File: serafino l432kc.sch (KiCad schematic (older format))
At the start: 31 parts, among them J1 USB_B_Micro, J2 Conn_01x14, J3 Conn_01x14, Q1 SI3401A-TP, SW1 SW_Push, SW2 SW_Push, U1 AP2112K-3.3, U2 USBLC6-2SC6, U3 STM32L432KCUx, Y1 32.768K

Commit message: Avances
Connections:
- net BOOT0: no longer J2.13 (Pin_13)
- net EN: no longer J2.2 (Pin_2)
- net PA8: now also J2.13 (Pin_13); no longer J3.4 (Pin_4)
- net VHIGH: now also J2.2 (Pin_2); no longer J2.3 (Pin_3)
- net USB_D+ renamed CAN_TD
- net CAN_TD: now also J2.3 (Pin_3)
- net USB_D- renamed CAN_RD
- net CAN_RD: now also J3.4 (Pin_4)
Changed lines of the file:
@@
 Text GLabel 6700 4800 2    50   Input ~ 0
 SWCLK
-Text GLabel 6700 4600 2    50   Input ~ 0
+Text GLabel 7350 4700 2    50   Input ~ 0
 USB_D+
-Text GLabel 6700 4500 2    50   Input ~ 0
+Text GLabel 7350 4400 2    50   Input ~ 0
 USB_D-
 Text GLabel 5700 4800 0    50   Input ~ 0
@@
 	1    0    0    -1
 $EndComp
-Text GLabel 8750 3650 0    50   Input ~ 0
+Text GLabel 8750 3550 0    50   Input ~ 0
 VHIGH
 Text GLabel 8750 4750 0    50   Input ~ 0
 NRST
-Text GLabel 10250 3750 0    50   Input ~ 0
+Text GLabel 8750 4650 0    50   Input ~ 0
 PA8
 Text GLabel 8750 4050 0    50   Input ~ 0
@@
 Text GLabel 10250 3950 0    50   Input ~ 0
 SPI1_SS
-Text GLabel 8750 4250 0    50   Input ~ 0
-PB4
 Text GLabel 10250 4650 0    50   Input ~ 0
 LED0
@@
 Text GLabel 10250 4350 0    50   Input ~ 0
 SAI1_FS_B
-Text GLabel 8750 4550 0    50   Input ~ 0
-USART1_RX
-Text GLabel 8750 4450 0    50   Input ~ 0
-USART1_TX
 Text GLabel 10250 4250 0    50   Input ~ 0
 SPI1_SCK
@@
 Wire Wire Line
 	8500 3450 8750 3450
-Text GLabel 8750 4650 0    50   Input ~ 0
-BOOT0
 $Comp
 L Device:R_Small R3
@@
 Text GLabel 8750 4150 0    50   Input ~ 0
 SAI1_SCK_B
-Text GLabel 8750 3550 0    50   Input ~ 0
-EN
 Wire Wire Line
 	2250 4600 2900 4600
@@
 Text GLabel 5700 4700 0    50   Input ~ 0
 SAI1_SD_B
-Text GLabel 8750 4350 0    50   Input ~ 0
-SAI1_SD_B
-$Comp
-L power:+3.3V #PWR?
+$Comp
+L power:+3.3V #PWR0107
 U 1 1 6018DE27
 P 3850 5700
-F 0 "#PWR?" H 3850 5550 50  0001 C CNN
+F 0 "#PWR0107" H 3850 5550 50  0001 C CNN
 F 1 "+3.3V" H 3865 5873 50  0000 C CNN
 F 2 "" H 3850 5700 50  0001 C CNN
@@
 Text Notes 1500 6100 0    50   ~ 0
 * LED for Native \nDFU Mode Indicator
+Text GLabel 8750 4250 0    50   Input ~ 0
+PB4
+Text GLabel 8750 4350 0    50   Input ~ 0
+SAI1_SD_B
+Text GLabel 8750 4450 0    50   Input ~ 0
+USART1_TX
+Text GLabel 8750 4550 0    50   Input ~ 0
+USART1_RX
+Text GLabel 8750 3650 0    50   Input ~ 0
+CAN_TD
+Text GLabel 10250 3750 0    50   Input ~ 0
+CAN_RD
+Wire Wire Line
+	7350 4400 7250 4400
+Wire Wire Line
+	7250 4400 7250 4500
+Wire Wire Line
+	7250 4500 6700 4500
+Wire Wire Line
+	7350 4700 7250 4700
+Wire Wire Line
+	7250 4700 7250 4600
+Wire Wire Line
+	7250 4600 6700 4600
+Text GLabel 7350 4850 2    50   Input ~ 0
+CAN_TD
+Text GLabel 7350 4250 2    50   Input ~ 0
+CAN_RD
+Wire Wire Line
+	7350 4250 7250 4250
+Wire Wire Line
+	7250 4250 7250 4400
+Connection ~ 7250 4400
+Wire Wire Line
+	7350 4850 7250 4850
+Wire Wire Line
+	7250 4850 7250 4700
+Connection ~ 7250 4700
 $EndSCHEMATC

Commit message: Finished back labels
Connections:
- net EN: no longer names the net of R5.2, U1.3 (EN)
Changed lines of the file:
@@
 Wire Wire Line
 	2500 1850 2500 1700
-Text GLabel 2500 1950 3    50   Input ~ 0
-EN
-Wire Wire Line
-	2500 1950 2500 1850
-Connection ~ 2500 1850
 Wire Wire Line
 	8000 3650 8000 3750

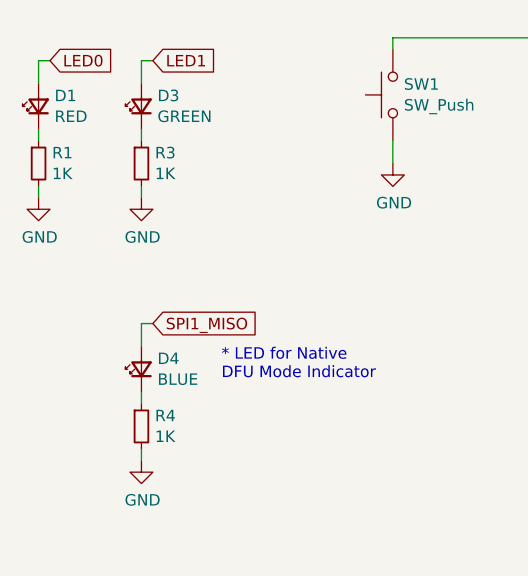
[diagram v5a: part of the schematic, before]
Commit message: Adjusted LED resistor values, changed BOOT0 to PA0 in silk screen.
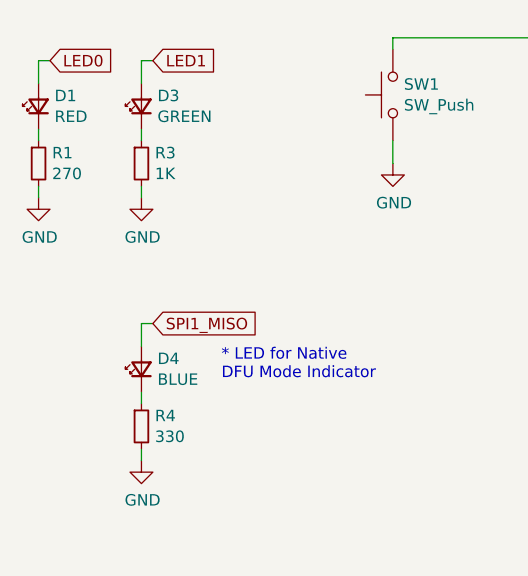
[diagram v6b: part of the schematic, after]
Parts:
- R1: value 1K -> 270
- R4: value 1K -> 330
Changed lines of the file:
@@
 P 700 5150
 F 0 "R1" H 759 5196 50  0000 L CNN
-F 1 "1K" H 759 5105 50  0000 L CNN
+F 1 "270" H 759 5105 50  0000 L CNN
 F 2 "Resistor_SMD:R_0603_1608Metric" H 700 5150 50  0001 C CNN
 F 3 "~" H 700 5150 50  0001 C CNN
@@
 P 1150 6300
 F 0 "R4" H 1209 6346 50  0000 L CNN
-F 1 "1K" H 1209 6255 50  0000 L CNN
+F 1 "330" H 1209 6255 50  0000 L CNN
 F 2 "Resistor_SMD:R_0603_1608Metric" H 1150 6300 50  0001 C CNN
 F 3 "~" H 1150 6300 50  0001 C CNN

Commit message: Led Specs
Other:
- note added: "* LED for Native DFU Mode Indicator\n* Max Source = 10ma"
- note added: "* Max Source = 17ma"
- note added: "* Max Source = 8ma"
- note added: "ATTENTION:\nEach pin can source up to 20ma*. \nAll pins can source up to 100ma in total.\n\n*"
- note removed: "* LED for Native \nDFU Mode Indicator"
- moved on the sheet: D3, D4, R3, R4
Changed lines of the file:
@@
 encoding utf-8
 Sheet 1 1
-Title ""
-Date ""
-Rev ""
-Comp ""
-Comment1 ""
+Title "Seraph L432KC"
+Date "2021-02-04"
+Rev "1.0"
+Comp "MATERIAM"
+Comment1 "Breakout board for STM32L432KC"
 Comment2 ""
 Comment3 ""
@@
 L Device:R_Small R3
 U 1 1 5FD4E68B
-P 1150 5150
-F 0 "R3" H 1209 5196 50  0000 L CNN
-F 1 "1K" H 1209 5105 50  0000 L CNN
-F 2 "Resistor_SMD:R_0603_1608Metric" H 1150 5150 50  0001 C CNN
-F 3 "~" H 1150 5150 50  0001 C CNN
-F 4 "RC0603FR-071KL" H 1150 5150 50  0001 C CNN "Part No."
-	1    1150 5150
+P 700 6200
+F 0 "R3" H 759 6246 50  0000 L CNN
+F 1 "1K" H 759 6155 50  0000 L CNN
+F 2 "Resistor_SMD:R_0603_1608Metric" H 700 6200 50  0001 C CNN
+F 3 "~" H 700 6200 50  0001 C CNN
+F 4 "RC0603FR-071KL" H 700 6200 50  0001 C CNN "Part No."
+	1    700  6200
 	1    0    0    -1
 $EndComp
@@
 L Device:LED_Small D3
 U 1 1 5FD4E887
-P 1150 4900
-F 0 "D3" V 1196 4830 50  0000 R CNN
-F 1 "GREEN" V 1105 4830 50  0000 R CNN
-F 2 "LED_SMD:LED_0603_1608Metric" V 1150 4900 50  0001 C CNN
-F 3 "~" V 1150 4900 50  0001 C CNN
-F 4 "155060GS75300" H 1150 4900 50  0001 C CNN "Part No."
-	1    1150 4900
+P 700 5950
+F 0 "D3" V 746 5880 50  0000 R CNN
+F 1 "GREEN" V 655 5880 50  0000 R CNN
+F 2 "LED_SMD:LED_0603_1608Metric" V 700 5950 50  0001 C CNN
+F 3 "~" V 700 5950 50  0001 C CNN
+F 4 "155060GS75300" H 700 5950 50  0001 C CNN "Part No."
+	1    700  5950
 	0    -1   -1   0
 $EndComp
@@
 L power:GND #PWR0106
 U 1 1 5FD4EB85
-P 1150 5300
-F 0 "#PWR0106" H 1150 5050 50  0001 C CNN
-F 1 "GND" H 1155 5127 50  0000 C CNN
-F 2 "" H 1150 5300 50  0001 C CNN
-F 3 "" H 1150 5300 50  0001 C CNN
-	1    1150 5300
+P 700 6350
+F 0 "#PWR0106" H 700 6100 50  0001 C CNN
+F 1 "GND" H 705 6177 50  0000 C CNN
+F 2 "" H 700 6350 50  0001 C CNN
+F 3 "" H 700 6350 50  0001 C CNN
+	1    700  6350
 	1    0    0    -1
 $EndComp
@@
 L Device:R_Small R4
 U 1 1 5FD4ED72
-P 1150 6300
-F 0 "R4" H 1209 6346 50  0000 L CNN
-F 1 "330" H 1209 6255 50  0000 L CNN
-F 2 "Resistor_SMD:R_0603_1608Metric" H 1150 6300 50  0001 C CNN
-F 3 "~" H 1150 6300 50  0001 C CNN
-F 4 "RC0603FR-071KL" H 1150 6300 50  0001 C CNN "Part No."
-	1    1150 6300
+P 700 7250
+F 0 "R4" H 759 7296 50  0000 L CNN
+F 1 "330" H 759 7205 50  0000 L CNN
+F 2 "Resistor_SMD:R_0603_1608Metric" H 700 7250 50  0001 C CNN
+F 3 "~" H 700 7250 50  0001 C CNN
+F 4 "RC0603FR-071KL" H 700 7250 50  0001 C CNN "Part No."
+	1    700  7250
 	1    0    0    -1
 $EndComp
@@
 L power:GND #PWR0108
 U 1 1 5FD4F1E4
-P 1150 6450
-F 0 "#PWR0108" H 1150 6200 50  0001 C CNN
-F 1 "GND" H 1155 6277 50  0000 C CNN
-F 2 "" H 1150 6450 50  0001 C CNN
-F 3 "" H 1150 6450 50  0001 C CNN
-	1    1150 6450
+P 700 7400
+F 0 "#PWR0108" H 700 7150 50  0001 C CNN
+F 1 "GND" H 705 7227 50  0000 C CNN
+F 2 "" H 700 7400 50  0001 C CNN
+F 3 "" H 700 7400 50  0001 C CNN
+	1    700  7400
 	1    0    0    -1
 $EndComp
@@
 L Device:LED_Small D4
 U 1 1 5FD4F3F3
-P 1150 6050
-F 0 "D4" V 1196 5980 50  0000 R CNN
-F 1 "BLUE" V 1105 5980 50  0000 R CNN
-F 2 "LED_SMD:LED_0603_1608Metric" V 1150 6050 50  0001 C CNN
-F 3 "~" V 1150 6050 50  0001 C CNN
-F 4 "155060BS75300" H 1150 6050 50  0001 C CNN "Part No."
-	1    1150 6050
+P 700 7000
+F 0 "D4" V 746 6930 50  0000 R CNN
+F 1 "BLUE" V 655 6930 50  0000 R CNN
+F 2 "LED_SMD:LED_0603_1608Metric" V 700 7000 50  0001 C CNN
+F 3 "~" V 700 7000 50  0001 C CNN
+F 4 "155060BS75300" H 700 7000 50  0001 C CNN "Part No."
+	1    700  7000
 	0    -1   -1   0
 $EndComp
 Wire Wire Line
-	1150 5000 1150 5050
-Wire Wire Line
-	1150 6150 1150 6200
-Wire Wire Line
-	1150 5250 1150 5300
-Wire Wire Line
-	1150 6400 1150 6450
-Text GLabel 1200 4700 2    50   Input ~ 0
+	700  6050 700  6100
+Wire Wire Line
+	700  7100 700  7150
+Wire Wire Line
+	700  6300 700  6350
+Wire Wire Line
+	700  7350 700  7400
+Text GLabel 750  5750 2    50   Input ~ 0
 LED1
 Wire Wire Line
-	1200 4700 1150 4700
-Wire Wire Line
-	1150 4700 1150 4800
-Wire Wire Line
-	1200 5850 1150 5850
-Wire Wire Line
-	1150 5850 1150 5950
+	750  5750 700  5750
+Wire Wire Line
+	700  5750 700  5850
+Wire Wire Line
+	750  6800 700  6800
+Wire Wire Line
+	700  6800 700  6900
 Connection ~ 1450 1400
 Wire Wire Line
@@
 Wire Wire Line
 	3850 6450 4050 6450
-Text GLabel 1200 5850 2    50   Input ~ 0
+Text GLabel 750  6800 2    50   Input ~ 0
 SPI1_MISO
-Text Notes 1500 6100 0    50   ~ 0
-* LED for Native \nDFU Mode Indicator
+Text Notes 1100 7150 0    50   ~ 0
+* LED for Native DFU Mode Indicator\n* Max Source = 10ma
 Text GLabel 8750 4250 0    50   Input ~ 0
 PB4
@@
 	7250 4850 7250 4700
 Connection ~ 7250 4700
+Text Notes 1100 6100 0    50   ~ 0
+* Max Source = 17ma
+Text Notes 1050 5150 0    50   ~ 0
+* Max Source = 8ma
+Text Notes 9300 5550 0    50   ~ 0
+ATTENTION:\nEach pin can source up to 20ma*. \nAll pins can source up to 100ma in total.\n\n*
 $EndSCHEMATC

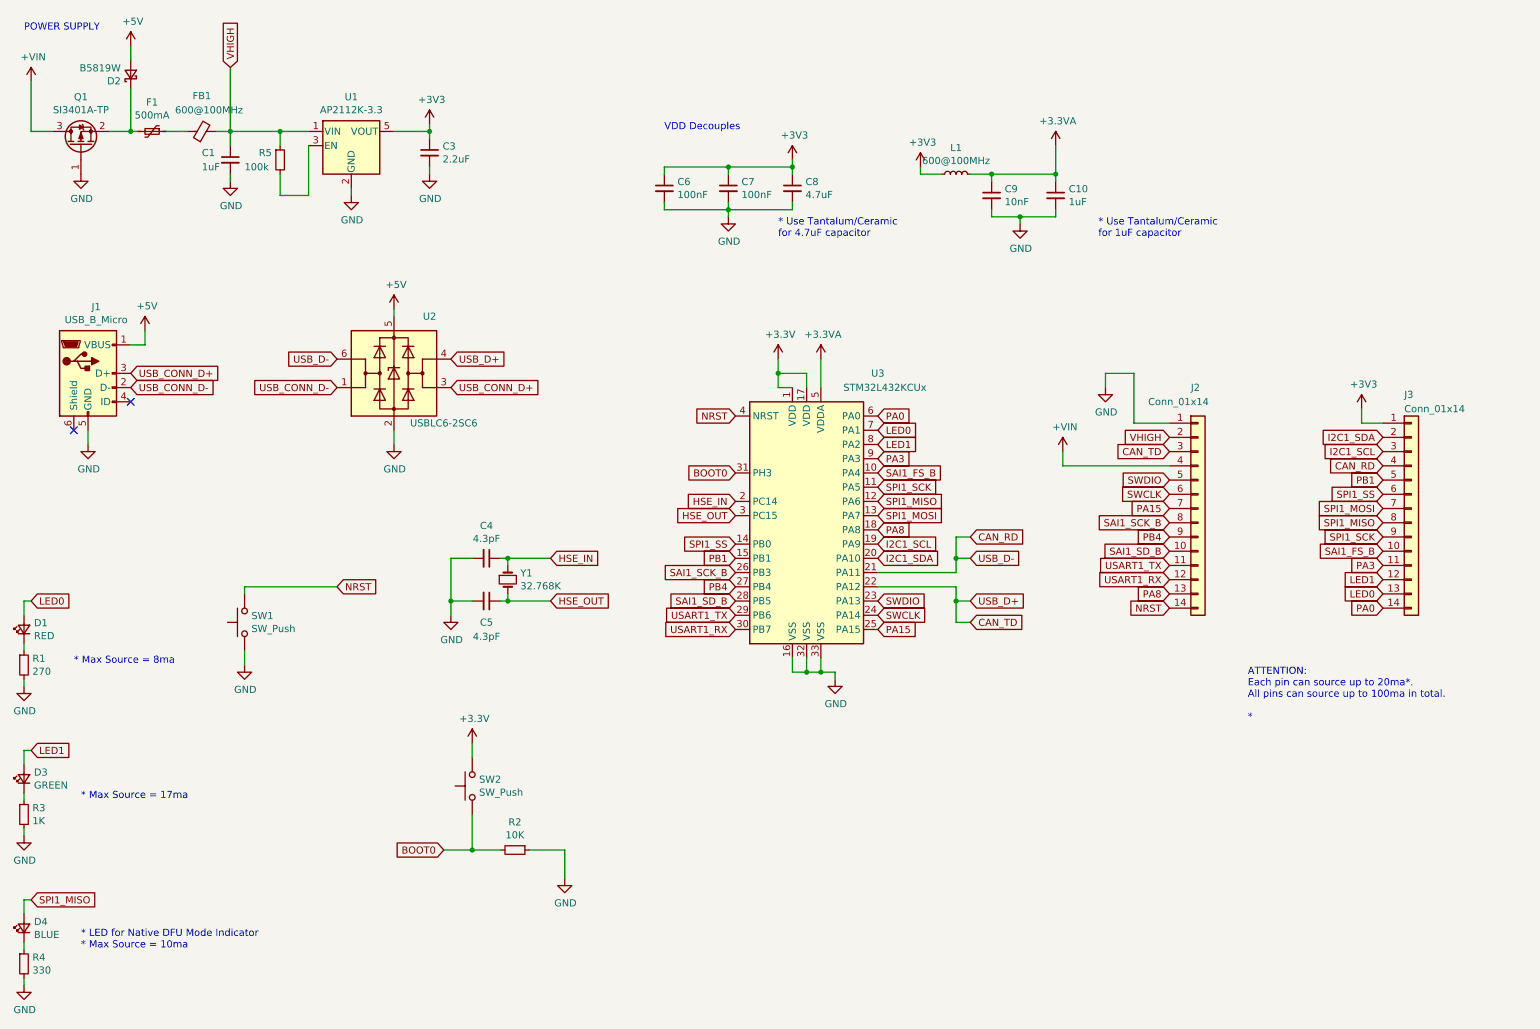
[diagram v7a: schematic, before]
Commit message: Disconnected LED2 from MISO since PA2 (LED1) is already on in DFU mode
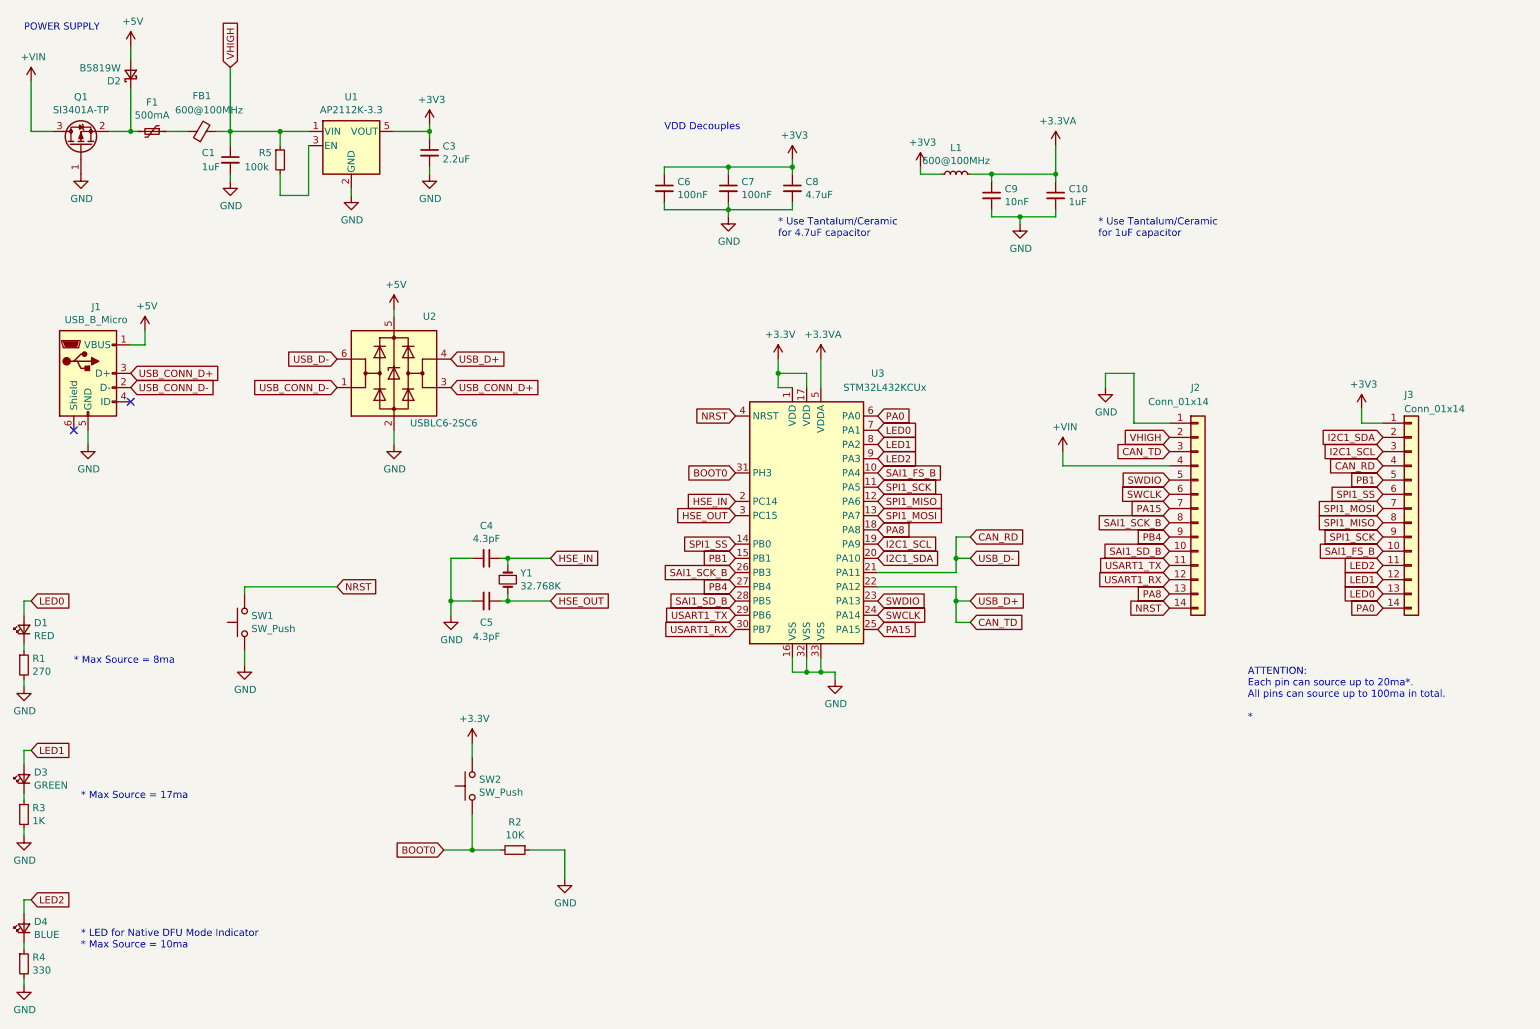
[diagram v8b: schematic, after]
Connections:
- net SPI1_MISO: no longer D4.2 (A)
- net PA3 renamed LED2
- net LED2: now also D4.2 (A)
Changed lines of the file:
@@
 $EndComp
 Text GLabel 6700 3700 2    50   Input ~ 0
-PA3
+LED2
 Text GLabel 6700 3600 2    50   Input ~ 0
 LED1
@@
 LED1
 Text GLabel 10250 4450 0    50   Input ~ 0
-PA3
+LED2
 Text GLabel 10250 4050 0    50   Input ~ 0
 SPI1_MOSI
@@
 	3850 6450 4050 6450
 Text GLabel 750  6800 2    50   Input ~ 0
-SPI1_MISO
+LED2
 Text Notes 1100 7150 0    50   ~ 0
 * LED for Native DFU Mode Indicator\n* Max Source = 10ma
